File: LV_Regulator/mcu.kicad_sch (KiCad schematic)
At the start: 58 parts, among them J5 SWD, J6 2169890001, U2 STM32F103C8Tx, U3 25CSM04xxSN, Y1 32.768kHz, Y2 8MHz

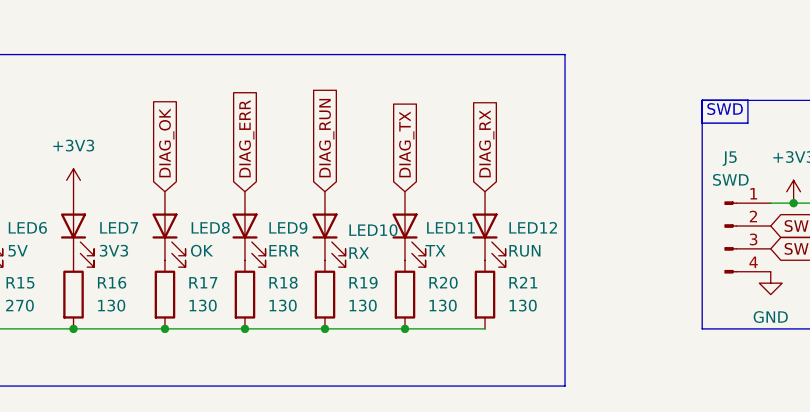
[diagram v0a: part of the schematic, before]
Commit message: Initial Routing for tje LV_Regulator control portion
Changes to the schematic were made for simpler routing
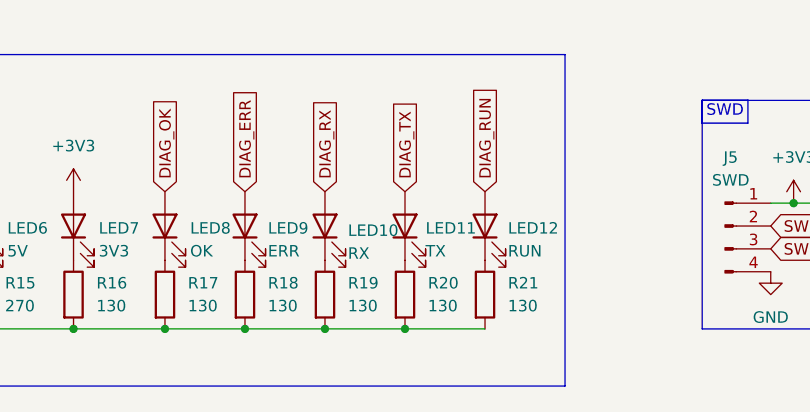
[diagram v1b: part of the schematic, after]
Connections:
- net DIAG_RUN: now also LED12.2 (A); no longer LED10.2 (A)
- net DIAG_RX: now also LED10.2 (A); no longer LED12.2 (A)

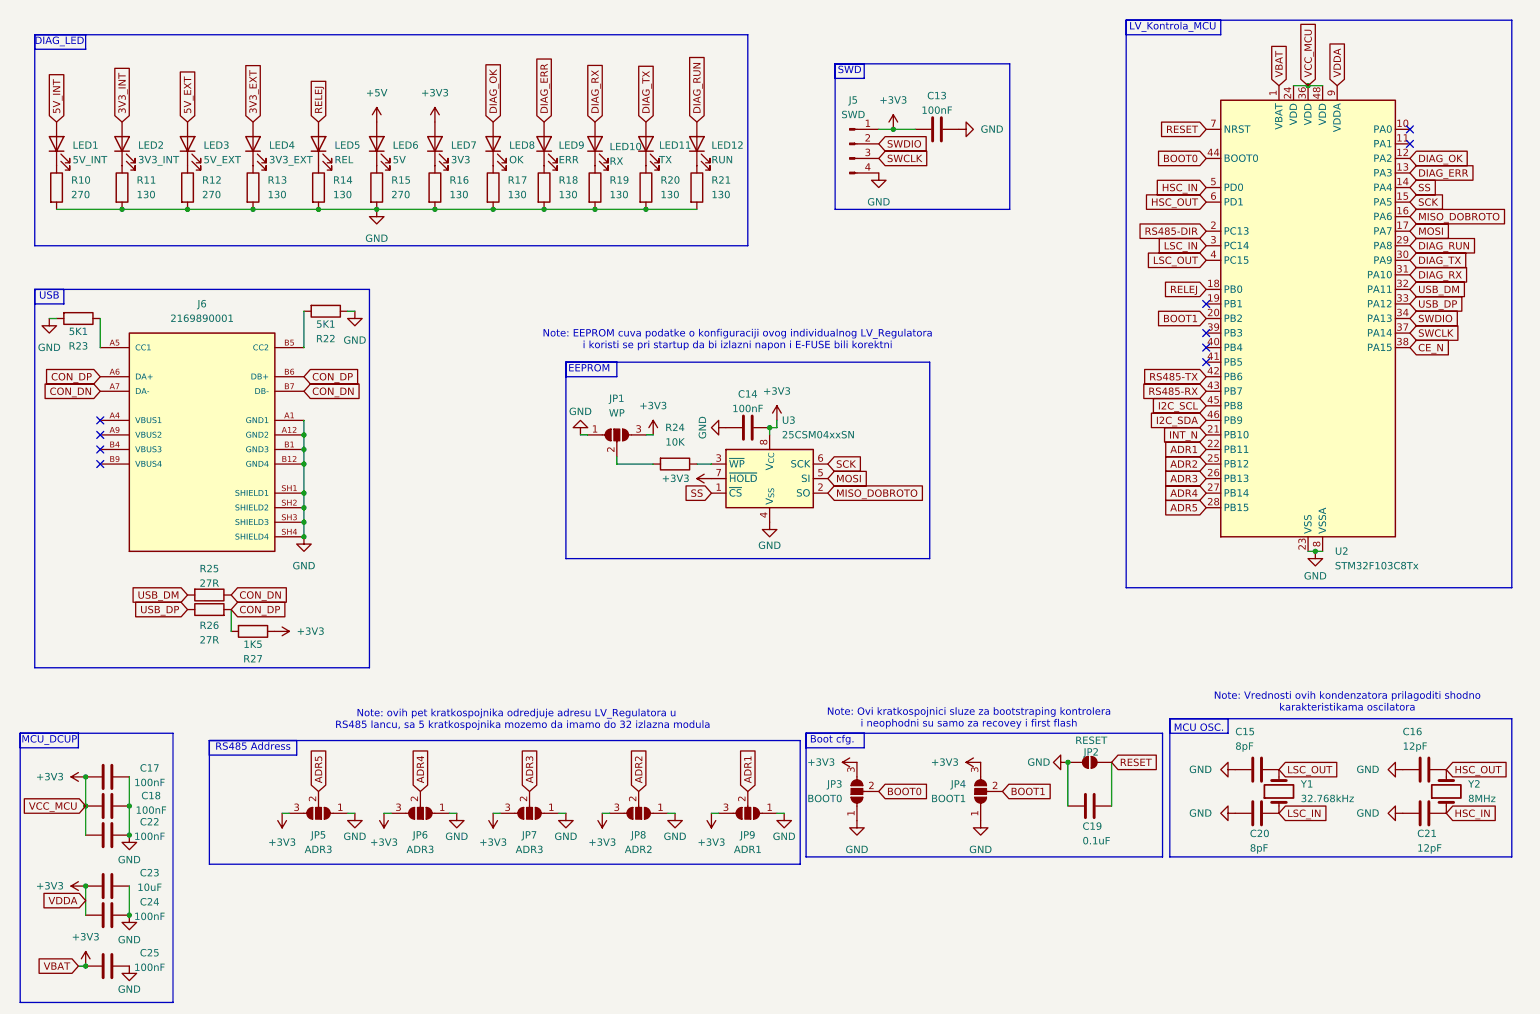
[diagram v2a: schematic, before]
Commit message: Redesigned the control section of the LV_Regulator
The routing of the control section was redone completely, LED's were labeled with their function, some signals were renamed for consistency, removed redundant testpoints, removed names of testpoints, changed configuration jumpers to have human reada
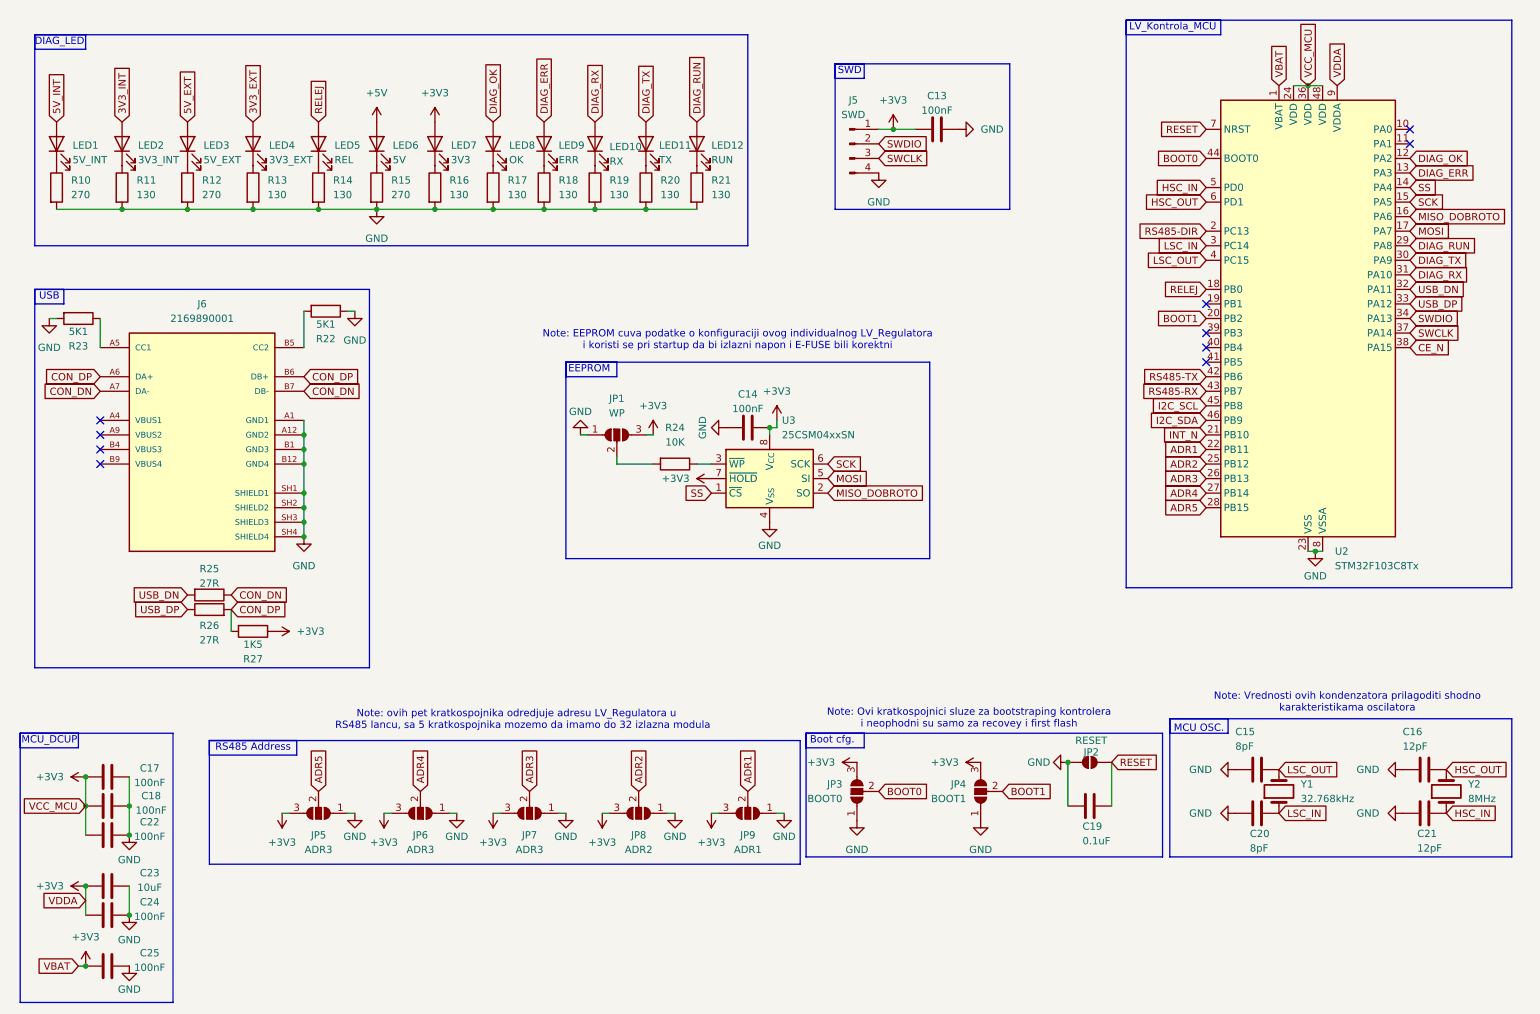
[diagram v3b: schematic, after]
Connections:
- net USB_DM renamed USB_DN
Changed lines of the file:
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@@
 		)
 	)
-	(global_label "USB_DM"
+	(global_label "USB_DN"
 		(shape input)
 		(at 264.16 66.04 0)
@@
 		)
 		(property "Intersheetrefs" "${INTERSHEET_REFS}"
-			(at 274.6442 66.04 0)
+			(at 274.5233 66.04 0)
 			(hide yes)
 			(show_name no)
@@
 		)
 	)
-	(global_label "USB_DM"
+	(global_label "USB_DN"
 		(shape input)
 		(at 50.8 119.38 180)
@@
 		)
 		(property "Intersheetrefs" "${INTERSHEET_REFS}"
-			(at 40.3158 119.38 0)
-			(hide yes)
-			(show_name no)
+			(at 40.4367 119.38 0)
+			(hide yes)
+			(show_name no)
